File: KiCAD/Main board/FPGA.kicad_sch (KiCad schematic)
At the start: 1 part

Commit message: Worked on main board design
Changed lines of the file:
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@@
     (effects (font (size 1.27 1.27) bold) (justify left bottom))
+  )
+  (hierarchical_label "BCK_ADC_CH1_2" (shape input) (at 29.21 116.84 0) (fields_autoplaced)
+    (effects (font (size 1.27 1.27)) (justify left))
+  )
+  (hierarchical_label "LRCK_ADC_CH1_2" (shape input) (at 29.21 114.3 0) (fields_autoplaced)
+    (effects (font (size 1.27 1.27)) (justify left))
+  )
+  (hierarchical_label "INPUT_SELECTOR_RELAY_CH1" (shape output) (at 29.21 124.46 0) (fields_autoplaced)
+    (effects (font (size 1.27 1.27)) (justify left))
   )
   (hierarchical_label "AMUTEI_DAC_CH5_6" (shape output) (at 208.28 100.33 0) (fields_autoplaced)
@@
   )
   (hierarchical_label "DIN_DAC_CH3_4" (shape output) (at 208.28 72.39 0) (fields_autoplaced)
+    (effects (font (size 1.27 1.27)) (justify left))
+  )
+  (hierarchical_label "DATA_ADC_CH1_2" (shape input) (at 29.21 119.38 0) (fields_autoplaced)
     (effects (font (size 1.27 1.27)) (justify left))
   )
@@
     (effects (font (size 1.27 1.27)) (justify left))
   )
+  (hierarchical_label "SCKI_ADC_CH1_2" (shape input) (at 29.21 111.76 0) (fields_autoplaced)
+    (effects (font (size 1.27 1.27)) (justify left))
+  )
   (hierarchical_label "AMUTEI_DAC_CH1_2" (shape output) (at 208.28 59.69 0) (fields_autoplaced)
     (effects (font (size 1.27 1.27)) (justify left))
@@
     (effects (font (size 1.27 1.27)) (justify left))
   )
+  (hierarchical_label "INPUT_SELECTOR_RELAY_CH2" (shape output) (at 29.21 127 0) (fields_autoplaced)
+    (effects (font (size 1.27 1.27)) (justify left))
+  )

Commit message: Worked in main board
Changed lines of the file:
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@@
     (effects (font (size 1.27 1.27) bold) (justify left bottom))
   )
-  (hierarchical_label "BCK_ADC_CH1_2" (shape input) (at 29.21 116.84 0) (fields_autoplaced)
+  (hierarchical_label "BCK_ADC_CH1_2" (shape input) (at 29.21 115.57 0) (fields_autoplaced)
     (effects (font (size 1.27 1.27)) (justify left))
   )
-  (hierarchical_label "LRCK_ADC_CH1_2" (shape input) (at 29.21 114.3 0) (fields_autoplaced)
+  (hierarchical_label "LRCK_ADC_CH1_2" (shape input) (at 29.21 113.03 0) (fields_autoplaced)
     (effects (font (size 1.27 1.27)) (justify left))
   )
@@
     (effects (font (size 1.27 1.27)) (justify left))
   )
-  (hierarchical_label "DATA_ADC_CH1_2" (shape input) (at 29.21 119.38 0) (fields_autoplaced)
+  (hierarchical_label "DATA_ADC_CH1_2" (shape input) (at 29.21 118.11 0) (fields_autoplaced)
     (effects (font (size 1.27 1.27)) (justify left))
   )
@@
     (effects (font (size 1.27 1.27)) (justify left))
   )
+  (hierarchical_label "~{TXS0102_OE_CH1_2}" (shape output) (at 29.21 140.97 0) (fields_autoplaced)
+    (effects (font (size 1.27 1.27)) (justify left))
+  )
   (hierarchical_label "SDA_DAC_CH1_2" (shape bidirectional) (at 208.28 62.23 0) (fields_autoplaced)
     (effects (font (size 1.27 1.27)) (justify left))
   )
-  (hierarchical_label "SCKI_ADC_CH1_2" (shape input) (at 29.21 111.76 0) (fields_autoplaced)
+  (hierarchical_label "SCKI_ADC_CH1_2" (shape input) (at 29.21 110.49 0) (fields_autoplaced)
+    (effects (font (size 1.27 1.27)) (justify left))
+  )
+  (hierarchical_label "TXS0102_SCLK_CH1_2" (shape output) (at 29.21 135.89 0) (fields_autoplaced)
     (effects (font (size 1.27 1.27)) (justify left))
   )
@@
     (effects (font (size 1.27 1.27)) (justify left))
   )
+  (hierarchical_label "~{RST_ADC_CH1_2}" (shape output) (at 29.21 120.65 0) (fields_autoplaced)
+    (effects (font (size 1.27 1.27)) (justify left))
+  )
   (hierarchical_label "SDA_DAC_CH3_4" (shape bidirectional) (at 208.28 82.55 0) (fields_autoplaced)
     (effects (font (size 1.27 1.27)) (justify left))
@@
     (effects (font (size 1.27 1.27)) (justify left))
   )
+  (hierarchical_label "TXS0102_SDA_CH1_2" (shape bidirectional) (at 29.21 138.43 0) (fields_autoplaced)
+    (effects (font (size 1.27 1.27)) (justify left))
+  )

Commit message: Ad good as finilized the main board schematic
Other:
- note added: "-Checken of deze pin assignment mogelijk is dmv een test programma? -Checken hoe erg de crosstalk aanwezig is dmv een test programma?"
- note added: "I will make these last connections as soon as the PCB design is a bit further. Because of the flexibility of the FPGA, the PCB design can be made easier by choosing these connections wisely."
- note added: "UI"
- note added: "USB port of DE1-SOC board can be used as USB audio input."
- note removed: "-Checken of deze pin assignment mogelijk is dmv een test programma. -Checken hoe erg de crosstalk aanwezig is dmv een test programma."
- note removed: "Check symbol and footprint with someone else"
- note removed: "USB port of FPGA can be used as USB audio input"
- title: (none) -> AUDIO-DSP_MAIN_BOARD
- moved on the sheet: U8A, U8B

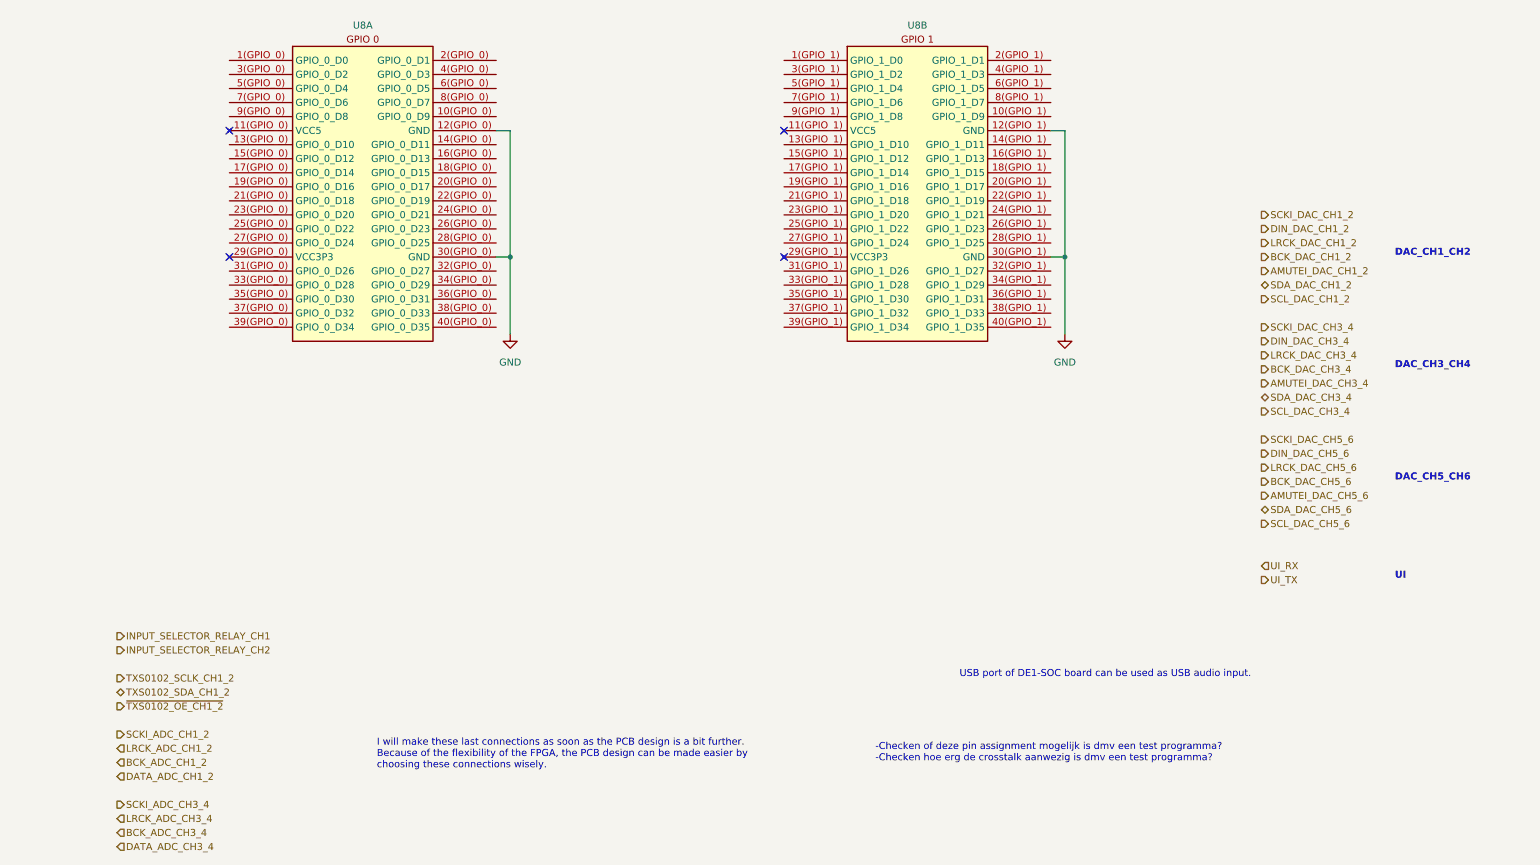
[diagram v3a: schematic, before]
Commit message: Finalizer main board schematic exept passive order links. Schematic ready for review
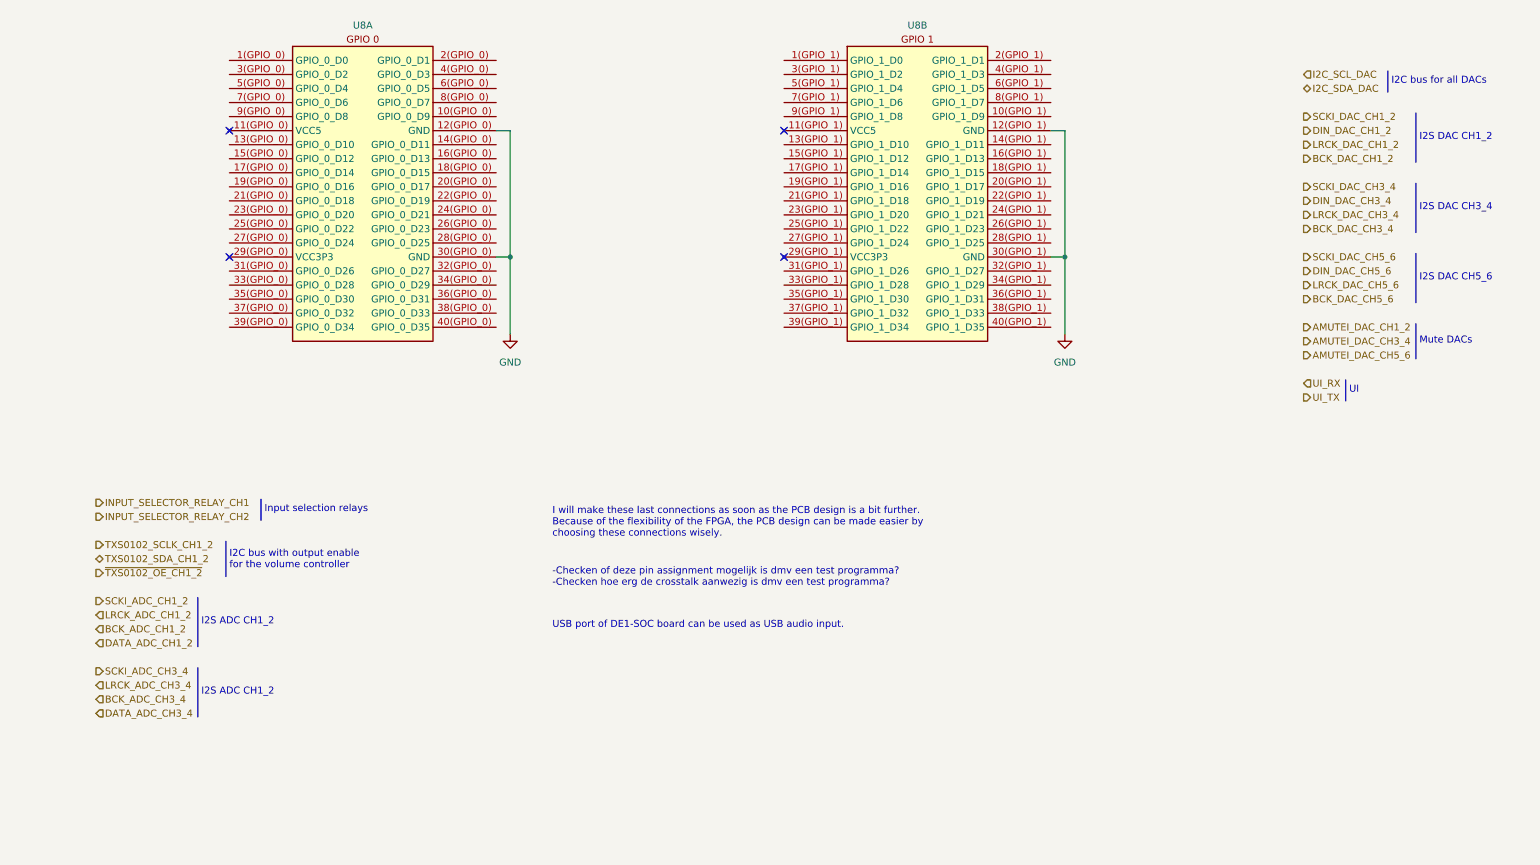
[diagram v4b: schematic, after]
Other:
- note added: "I2C bus for all DACs"
- note added: "I2C bus with output enable for the volume controller"
- note added: "I2S ADC CH1_2"
- note added: "I2S DAC CH1_2"
- note added: "I2S DAC CH3_4"
- note added: "I2S DAC CH5_6"
- note added: "Input selection relays"
- note added: "Mute DACs"
- note removed: "DAC_CH1_CH2"
- note removed: "DAC_CH3_CH4"
- note removed: "DAC_CH5_CH6"

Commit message: Main board
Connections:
- net AMUTEI_DAC_CH1_2: now also U8.33(GPIO_1) (GPIO_1_D28)
- net AMUTEI_DAC_CH3_4: now also U8.21(GPIO_1) (GPIO_1_D18)
- net AMUTEI_DAC_CH5_6: now also U8.9(GPIO_1) (GPIO_1_D8)
- net BCK_ADC_CH1_2: now also U8.9(GPIO_0) (GPIO_0_D8)
- net BCK_ADC_CH3_4: now also U8.19(GPIO_0) (GPIO_0_D16)
- net BCK_DAC_CH1_2: now also U8.27(GPIO_1) (GPIO_1_D24)
- net BCK_DAC_CH3_4: now also U8.17(GPIO_1) (GPIO_1_D14)
- net BCK_DAC_CH5_6: now also U8.5(GPIO_1) (GPIO_1_D4)
- net DATA_ADC_CH1_2: now also U8.13(GPIO_0) (GPIO_0_D10)
- net DATA_ADC_CH3_4: now also U8.21(GPIO_0) (GPIO_0_D18)
- net DIN_DAC_CH1_2: now also U8.25(GPIO_1) (GPIO_1_D22)
- net DIN_DAC_CH3_4: now also U8.15(GPIO_1) (GPIO_1_D12)
- net DIN_DAC_CH5_6: now also U8.3(GPIO_1) (GPIO_1_D2)
- net GND: now also U8.10(GPIO_0) (GPIO_0_D9), U8.10(GPIO_1) (GPIO_1_D9), U8.14(GPIO_0) (GPIO_0_D11), U8.14(GPIO_1) (GPIO_1_D11), U8.16(GPIO_0) (GPIO_0_D13), U8.16(GPIO_1) (GPIO_1_D13), U8.18(GPIO_0) (GPIO_0_D15), U8.18(GPIO_1) (GPIO_1_D15), U8.2(GPIO_0) (GPIO_0_D1), U8.2(GPIO_1) (GPIO_1_D1), U8.20(GPIO_0) (GPIO_0_D17), U8.20(GPIO_1) (GPIO_1_D17), U8.22(GPIO_0) (GPIO_0_D19), U8.22(GPIO_1) (GPIO_1_D19), U8.24(GPIO_0) (GPIO_0_D21), U8.24(GPIO_1) (GPIO_1_D21), U8.26(GPIO_0) (GPIO_0_D23), U8.26(GPIO_1) (GPIO_1_D23), U8.28(GPIO_0) (GPIO_0_D25), U8.28(GPIO_1) (GPIO_1_D25), U8.32(GPIO_0) (GPIO_0_D27), U8.32(GPIO_1) (GPIO_1_D27), U8.34(GPIO_0) (GPIO_0_D29), U8.34(GPIO_1) (GPIO_1_D29), U8.36(GPIO_0) (GPIO_0_D31), U8.36(GPIO_1) (GPIO_1_D31), U8.38(GPIO_0) (GPIO_0_D33), U8.38(GPIO_1) (GPIO_1_D33), U8.4(GPIO_0) (GPIO_0_D3), U8.4(GPIO_1) (GPIO_1_D3), U8.40(GPIO_0) (GPIO_0_D35), U8.40(GPIO_1) (GPIO_1_D35), U8.6(GPIO_0) (GPIO_0_D5), U8.6(GPIO_1) (GPIO_1_D5), U8.8(GPIO_0) (GPIO_0_D7), U8.8(GPIO_1) (GPIO_1_D7)
- net I2C_SCL_DAC: now also U8.35(GPIO_1) (GPIO_1_D30)
- net I2C_SDA_DAC: now also U8.37(GPIO_1) (GPIO_1_D32)
- net INPUT_SELECTOR_RELAY_CH1: now also U8.1(GPIO_0) (GPIO_0_D0)
- net INPUT_SELECTOR_RELAY_CH2: now also U8.3(GPIO_0) (GPIO_0_D2)
- net LRCK_ADC_CH1_2: now also U8.7(GPIO_0) (GPIO_0_D6)
- net LRCK_ADC_CH3_4: now also U8.17(GPIO_0) (GPIO_0_D14)
- net LRCK_DAC_CH1_2: now also U8.31(GPIO_1) (GPIO_1_D26)
- net LRCK_DAC_CH3_4: now also U8.19(GPIO_1) (GPIO_1_D16)
- net LRCK_DAC_CH5_6: now also U8.7(GPIO_1) (GPIO_1_D6)
- net SCKI_ADC_CH1_2: now also U8.5(GPIO_0) (GPIO_0_D4)
- net SCKI_ADC_CH3_4: now also U8.15(GPIO_0) (GPIO_0_D12)
- net SCKI_DAC_CH1_2: now also U8.23(GPIO_1) (GPIO_1_D20)
- net SCKI_DAC_CH3_4: now also U8.13(GPIO_1) (GPIO_1_D10)
- net SCKI_DAC_CH5_6: now also U8.1(GPIO_1) (GPIO_1_D0)
- net TXS0102_SCLK_CH1_2: now also U8.23(GPIO_0) (GPIO_0_D20)
- net TXS0102_SDA_CH1_2: now also U8.25(GPIO_0) (GPIO_0_D22)
- net UI_RX: now also U8.37(GPIO_0) (GPIO_0_D32)
- net UI_TX: now also U8.39(GPIO_0) (GPIO_0_D34)
- net ~{TXS0102_OE_CH1_2}: now also U8.27(GPIO_0) (GPIO_0_D24)
- no-connect marks 4 -> 8
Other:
- note added: "I2S ADC CH3_4"
- note added: "Mute DAC CH1_2"
- note added: "Mute DAC CH3_4"
- note added: "Mute DAC CH5_6"
- note removed: "I will make these last connections as soon as the PCB design is a bit further. Because of the flexibility of the FPGA, the PCB design can be made easier by choosing these connections wisely."
- note removed: "Mute DACs"
- moved on the sheet: U8A, U8B

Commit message: Schematic send to Ralph for review
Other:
- note removed: "-Checken of deze pin assignment mogelijk is dmv een test programma? -Checken hoe erg de crosstalk aanwezig is dmv een test programma?"
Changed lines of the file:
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@@
     (stroke (width 0) (type default))
-  )
-  (text "-Checken of deze pin assignment mogelijk is dmv een test programma?\n-Checken hoe erg de crosstalk aanwezig is dmv een test programma?"
-    (at 107.95 116.84 0)
-    (effects (font (size 1.27 1.27) (color 200 0 200 1)) (justify left bottom))
   )
   (text "I2S ADC CH1_2" (at 135.89 31.75 0)
@@
   )
   (text "USB port of DE1-SOC board can be used as USB audio input."
-    (at 107.95 124.46 0)
+    (at 12.7 78.74 0)
     (effects (font (size 1.27 1.27)) (justify left bottom))
   )

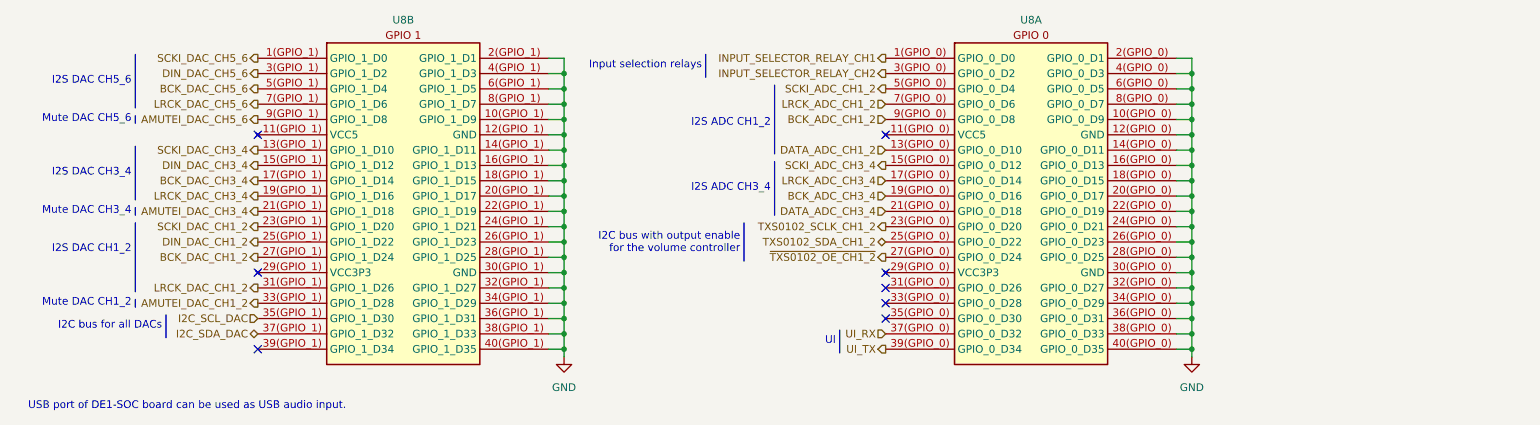
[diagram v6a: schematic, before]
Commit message: Added rotary encoder and pull-up
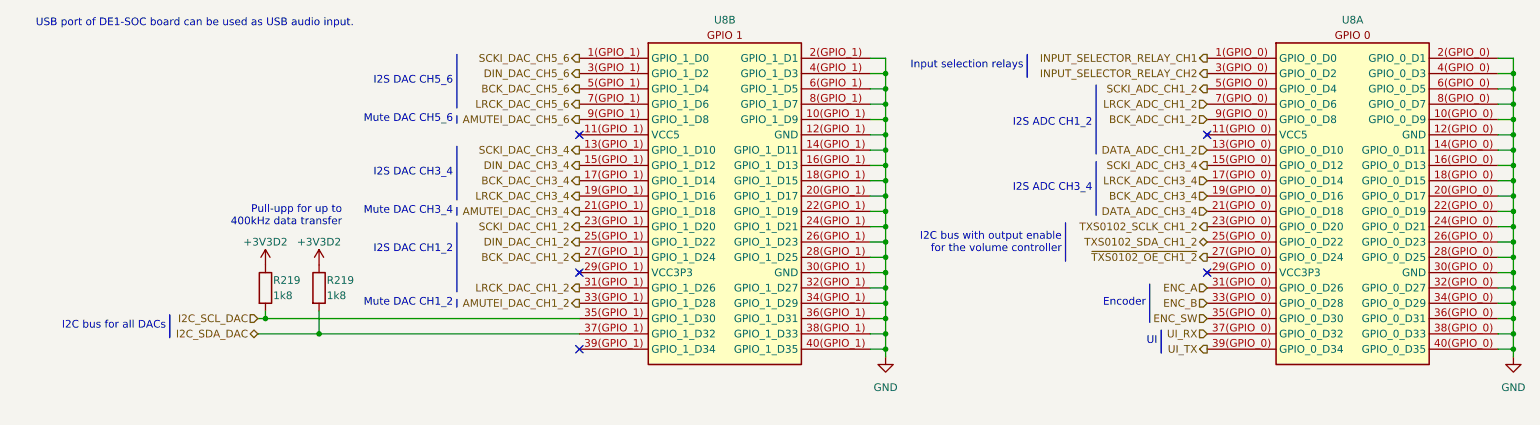
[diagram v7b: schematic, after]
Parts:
- added R219 (x2): 1k8, Resistor_SMD:R_0402_1005Metric, symbol Device:R
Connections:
- net I2C_SCL_DAC: now also R219.2
- net I2C_SDA_DAC: now also R219.2
- net ENC_A: now reaches U8.31(GPIO_0) (GPIO_0_D26)
- net ENC_B: now reaches U8.33(GPIO_0) (GPIO_0_D28)
- net ENC_SW: now reaches U8.35(GPIO_0) (GPIO_0_D30)
- new net +3V3D2: R219.1, R219.1
- no-connect marks 8 -> 5
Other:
- note added: "Encoder"
- note added: "Pull-upp for up to 400kHz data transfer"
- moved on the sheet: U8A, U8B

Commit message: PCB finished + gerber
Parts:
- removed R219 (x2): 1k8, Resistor_SMD:R_0402_1005Metric, symbol Device:R
- added R219 (x2): 1k8, Resistor_SMD:R_0402_1005Metric, symbol Device:R
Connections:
- net +3V3D2: now also R219.1, R219.1
- net AMUTEI_DAC_CH3_4: now also U8.35(GPIO_1) (GPIO_1_D30); no longer U8.21(GPIO_1) (GPIO_1_D18)
- net I2C_SCL_DAC: now also U8.37(GPIO_1) (GPIO_1_D32), R219.2; no longer U8.35(GPIO_1) (GPIO_1_D30)
- net I2C_SDA_DAC: now also U8.21(GPIO_1) (GPIO_1_D18), R219.2; no longer U8.37(GPIO_1) (GPIO_1_D32)
